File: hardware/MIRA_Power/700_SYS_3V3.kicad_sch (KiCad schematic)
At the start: 24 parts, among them Q701 BSS138N, U701 LM76005RNPR

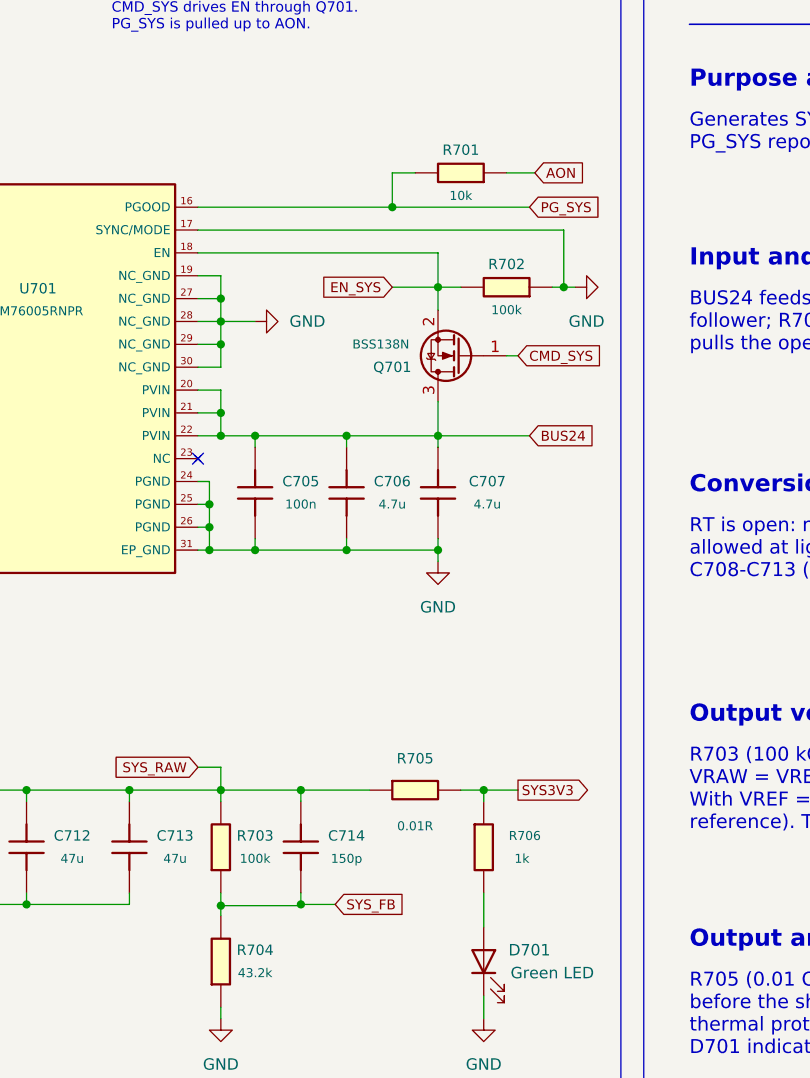
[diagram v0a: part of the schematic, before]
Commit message: Add high-load schematic candidate with CORE sense and revised N15 supply
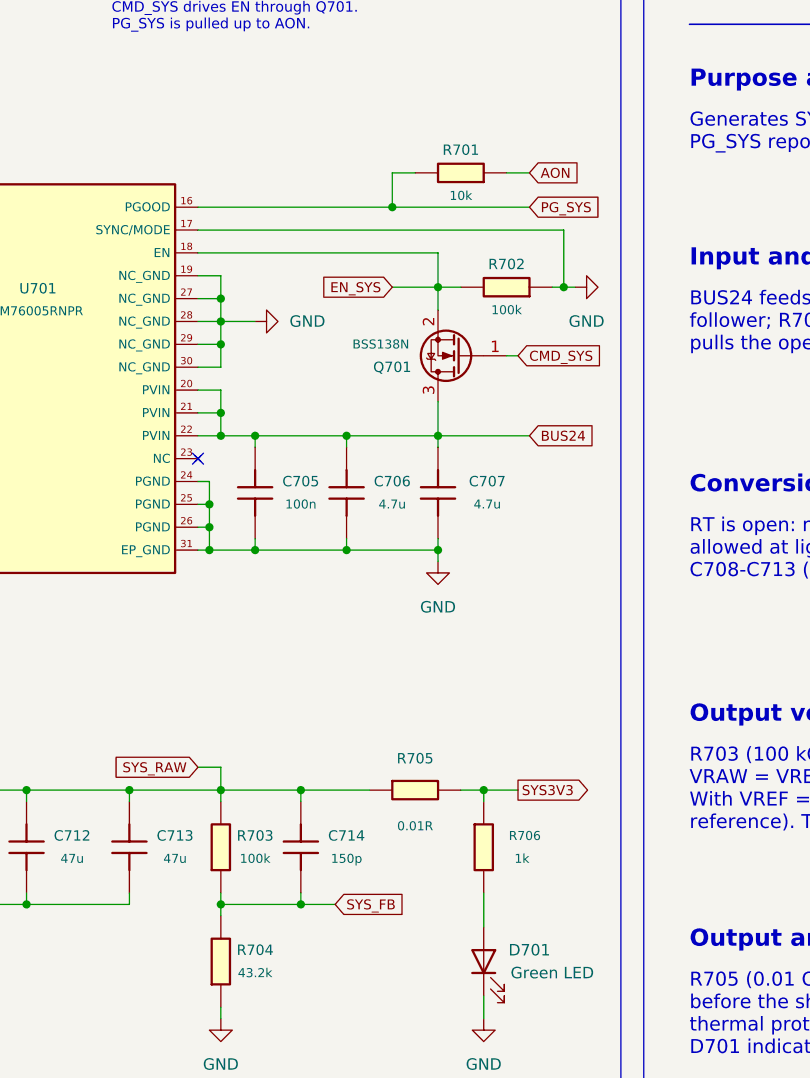
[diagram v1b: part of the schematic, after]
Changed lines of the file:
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@@
 	)
 	(junction
-		(at 104.14 133.49)
+		(at 104.14 133.35)
 		(diameter 0)
 		(color 0 0 0 0)
@@
 	(wire
 		(pts
-			(xy 139.03 52.07) (xy 135.89 52.07)
+			(xy 138.43 52.07) (xy 135.89 52.07)
 		)
 		(stroke
@@
 	(wire
 		(pts
-			(xy 113.03 133.35) (xy 113.03 133.49)
+			(xy 113.03 133.35) (xy 113.03 133.35)
 		)
 		(stroke
@@
 	(wire
 		(pts
-			(xy 104.14 133.49) (xy 113.03 133.49)
+			(xy 104.14 133.35) (xy 113.03 133.35)
 		)
 		(stroke
@@
 	(wire
 		(pts
-			(xy 104.14 133.49) (xy 104.14 134.62)
+			(xy 104.14 133.35) (xy 104.14 134.62)
 		)
 		(stroke
@@
 	(wire
 		(pts
-			(xy 104.14 132.08) (xy 104.14 133.49)
+			(xy 104.14 132.08) (xy 104.14 133.35)
 		)
 		(stroke
@@
 	(global_label "AON"
 		(shape input)
-		(at 139.03 52.07 0)
+		(at 138.43 52.07 0)
 		(effects
 			(font
@@
 		)
 		(property "Intersheetrefs" "${INTERSHEET_REFS}"
-			(at 139.03 52.07 0)
+			(at 138.43 52.07 0)
 			(hide yes)
 			(show_name no)

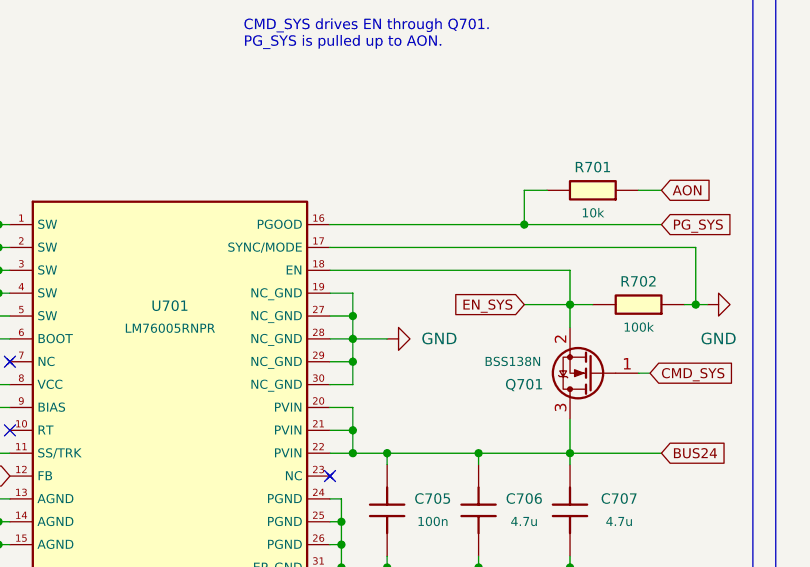
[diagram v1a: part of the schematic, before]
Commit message: Protect unpowered signal domains and qualify local supplies; retain startup and fault interlocks
MIRA-Startup-Patch: 7ffae17756ebcf923eff1212bb1aade8fbdfae03a9ca8ecebc69d3da3d3b4ba2
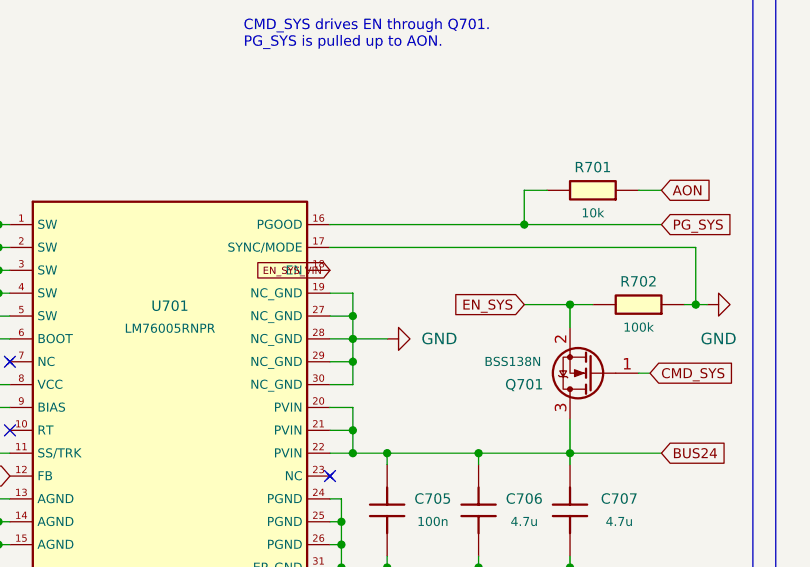
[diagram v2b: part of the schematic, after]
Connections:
- net EN_SYS: no longer U701.18 (EN)
- new net EN_SYS_VIN: U701.18 (EN)
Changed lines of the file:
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@@
 	(wire
 		(pts
-			(xy 128.27 60.96) (xy 128.27 64.77)
-		)
-		(stroke
-			(width 0)
-			(type default)
-		)
-	)
-	(wire
-		(pts
 			(xy 104.14 81.28) (xy 107.95 81.28)
 		)
@@
 	(wire
 		(pts
-			(xy 101.6 60.96) (xy 128.27 60.96)
-		)
-		(stroke
-			(width 0)
-			(type default)
-		)
-	)
-	(wire
-		(pts
 			(xy 101.6 66.04) (xy 104.14 66.04)
 		)
@@
 		)
 	)
+(global_label "EN_SYS_VIN" (shape input) (at 101.6 60.96 180) (effects (font (size 0.8 0.8)) (justify right)))
 )
